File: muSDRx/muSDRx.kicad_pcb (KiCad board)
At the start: 2 copper layers, 100 x 100 mm, 98 parts, among them CON1 SJ1-3523N, CON2 SJ1-3523N, J1 Conn_01x02_Male, J11 Conn_01x02_Male, J2 Conn_01x02_Male, J3 Conn_01x02_Male, J4 Conn_01x02_Male, J5 Conn_01x02_Male, J6 Conn_01x02_Male, J9 Conn_01x04_Male, P1 BNC, Q1 MMBT2222A-TP, SW1 SW_Push, SW2 SW_Push, SW3 Rotary_Encoder_Switch, U1 LCD1602, U2 Si5351A-B-GT, U3 SN74CBT3253, U4 BluePill, U5 LT6231 (or LM4562), U6 MC78M05_TO252, Y1 CX3225

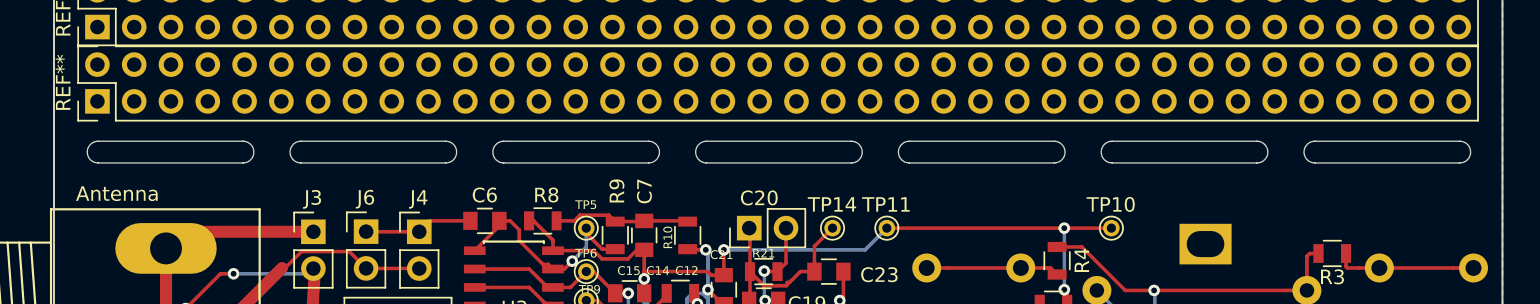
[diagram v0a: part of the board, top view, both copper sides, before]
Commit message: Added notes and C11-C15 value changes.
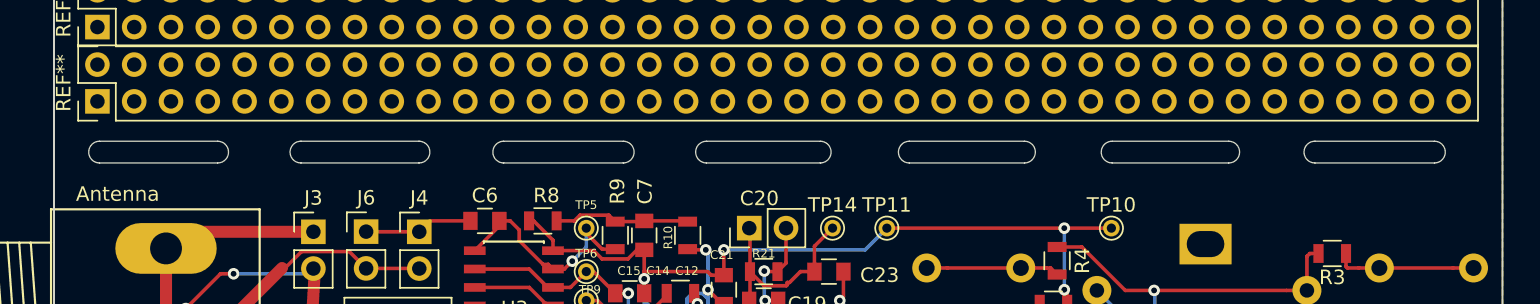
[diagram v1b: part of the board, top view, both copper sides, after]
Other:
- outline, holes or cut-outs redrawn
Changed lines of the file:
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@@
     (pad_to_mask_clearance 0.051)
     (solder_mask_min_width 0.25)
+    (pad_to_paste_clearance_ratio -0.2)
     (aux_axis_origin 0 0)
     (visible_elements FFFFFF7F)
@@
       (outputformat 1)
       (mirror false)
-      (drillshape 1)
+      (drillshape 0)
       (scaleselection 1)
       (outputdirectory ""))
@@
     )
   )
+  (gr_arc (start 61.3 95.5) (end 61.3 96.25) (angle -180) (layer Edge.Cuts) (width 0.05))
   (gr_text "Sound card" (at 144.9 113.3) (layer F.SilkS)
     (effects (font (size 1 1) (thickness 0.15)))
@@
   (gr_line (start 150 50) (end 150 150) (layer F.SilkS) (width 0.12))
   (gr_line (start 50 50) (end 150 50) (layer F.SilkS) (width 0.12))
-  (gr_arc (start 147.05 95.5) (end 147.05 96.25) (angle -180) (layer Edge.Cuts) (width 0.05))
+  (gr_arc (start 145.3 95.5) (end 145.3 96.25) (angle -180) (layer Edge.Cuts) (width 0.05))
   (gr_arc (start 137.05 95.5) (end 137.05 94.75) (angle -180) (layer Edge.Cuts) (width 0.05))
-  (gr_line (start 147.05 94.75) (end 137.05 94.75) (layer Edge.Cuts) (width 0.05))
-  (gr_line (start 137.05 96.25) (end 147.05 96.25) (layer Edge.Cuts) (width 0.05))
+  (gr_line (start 145.3 94.75) (end 137.05 94.75) (layer Edge.Cuts) (width 0.05))
+  (gr_line (start 137.05 96.25) (end 145.3 96.25) (layer Edge.Cuts) (width 0.05))
   (gr_arc (start 123.05 95.5) (end 123.05 94.75) (angle -180) (layer Edge.Cuts) (width 0.05))
-  (gr_line (start 133.05 94.75) (end 123.05 94.75) (layer Edge.Cuts) (width 0.05))
-  (gr_arc (start 133.05 95.5) (end 133.05 96.25) (angle -180) (layer Edge.Cuts) (width 0.05))
-  (gr_line (start 123.05 96.25) (end 133.05 96.25) (layer Edge.Cuts) (width 0.05))
+  (gr_line (start 131.1 94.75) (end 123.05 94.75) (layer Edge.Cuts) (width 0.05))
+  (gr_arc (start 131.1 95.5) (end 131.1 96.25) (angle -180) (layer Edge.Cuts) (width 0.05))
+  (gr_line (start 123.05 96.25) (end 131.1 96.25) (layer Edge.Cuts) (width 0.05))
   (gr_arc (start 109.05 95.5) (end 109.05 94.75) (angle -180) (layer Edge.Cuts) (width 0.05))
-  (gr_arc (start 119.05 95.5) (end 119.05 96.25) (angle -180) (layer Edge.Cuts) (width 0.05))
-  (gr_line (start 119.05 94.75) (end 109.05 94.75) (layer Edge.Cuts) (width 0.05))
-  (gr_line (start 109.05 96.25) (end 119.05 96.25) (layer Edge.Cuts) (width 0.05))
-  (gr_arc (start 105.05 95.5) (end 105.05 96.25) (angle -180) (layer Edge.Cuts) (width 0.05))
-  (gr_line (start 105.05 94.75) (end 95.05 94.75) (layer Edge.Cuts) (width 0.05))
+  (gr_arc (start 117 95.5) (end 117 96.25) (angle -180) (layer Edge.Cuts) (width 0.05))
+  (gr_line (start 117 94.75) (end 109.05 94.75) (layer Edge.Cuts) (width 0.05))
+  (gr_line (start 109.05 96.25) (end 117 96.25) (layer Edge.Cuts) (width 0.05))
+  (gr_arc (start 102.9 95.5) (end 102.9 96.25) (angle -180) (layer Edge.Cuts) (width 0.05))
+  (gr_line (start 102.9 94.75) (end 95.05 94.75) (layer Edge.Cuts) (width 0.05))
   (gr_arc (start 95.05 95.5) (end 95.05 94.75) (angle -180) (layer Edge.Cuts) (width 0.05))
-  (gr_line (start 95.05 96.25) (end 105.05 96.25) (layer Edge.Cuts) (width 0.05))
+  (gr_line (start 95.05 96.25) (end 102.9 96.25) (layer Edge.Cuts) (width 0.05))
   (gr_arc (start 81.05 95.5) (end 81.05 94.75) (angle -180) (layer Edge.Cuts) (width 0.05))
-  (gr_line (start 81.05 96.25) (end 91.05 96.25) (layer Edge.Cuts) (width 0.05))
-  (gr_line (start 91.05 94.75) (end 81.05 94.75) (layer Edge.Cuts) (width 0.05))
-  (gr_arc (start 91.05 95.5) (end 91.05 96.25) (angle -180) (layer Edge.Cuts) (width 0.05))
-  (gr_line (start 67.05 96.25) (end 77.05 96.25) (layer Edge.Cuts) (width 0.05))
-  (gr_line (start 77.05 94.75) (end 67.05 94.75) (layer Edge.Cuts) (width 0.05))
+  (gr_line (start 81.05 96.25) (end 89.3 96.25) (layer Edge.Cuts) (width 0.05))
+  (gr_line (start 89.3 94.75) (end 81.05 94.75) (layer Edge.Cuts) (width 0.05))
+  (gr_arc (start 89.3 95.5) (end 89.3 96.25) (angle -180) (layer Edge.Cuts) (width 0.05))
+  (gr_line (start 67.05 96.25) (end 75.2 96.25) (layer Edge.Cuts) (width 0.05))
+  (gr_line (start 75.2 94.75) (end 67.05 94.75) (layer Edge.Cuts) (width 0.05))
   (gr_arc (start 67.05 95.5) (end 67.05 94.75) (angle -180) (layer Edge.Cuts) (width 0.05))
-  (gr_arc (start 77.05 95.5) (end 77.05 96.25) (angle -180) (layer Edge.Cuts) (width 0.05))
-  (gr_line (start 53.05 96.25) (end 63.05 96.25) (layer Edge.Cuts) (width 0.05))
-  (gr_arc (start 53.05 95.5) (end 53.05 94.75) (angle -180) (layer Edge.Cuts) (width 0.05))
-  (gr_line (start 63.05 94.75) (end 53.05 94.75) (layer Edge.Cuts) (width 0.05))
-  (gr_arc (start 63.05 95.5) (end 63.05 96.25) (angle -180) (layer Edge.Cuts) (width 0.05))
+  (gr_arc (start 75.2 95.5) (end 75.2 96.25) (angle -180) (layer Edge.Cuts) (width 0.05))
+  (gr_line (start 53.15 96.25) (end 61.3 96.25) (layer Edge.Cuts) (width 0.05))
+  (gr_arc (start 53.15 95.5) (end 53.15 94.75) (angle -180) (layer Edge.Cuts) (width 0.05))
+  (gr_line (start 61.3 94.75) (end 53.15 94.75) (layer Edge.Cuts) (width 0.05))
   (gr_line (start 50.5 100) (end 150 100) (layer Margin) (width 0.15))
   (gr_line (start 50 150) (end 50 50) (layer Edge.Cuts) (width 0.05))
@@
     (connect_pads (clearance 0.508))
     (min_thickness 0.254)
-    (fill yes (arc_segments 32) (thermal_gap 0.508) (thermal_bridge_width 0.508))
+    (fill (arc_segments 32) (thermal_gap 0.508) (thermal_bridge_width 0.508))
     (polygon
       (pts
@@
     (connect_pads (clearance 0.508))
     (min_thickness 0.254)
-    (fill yes (arc_segments 32) (thermal_gap 0.508) (thermal_bridge_width 0.508))
+    (fill (arc_segments 32) (thermal_gap 0.508) (thermal_bridge_width 0.508))
     (polygon
       (pts

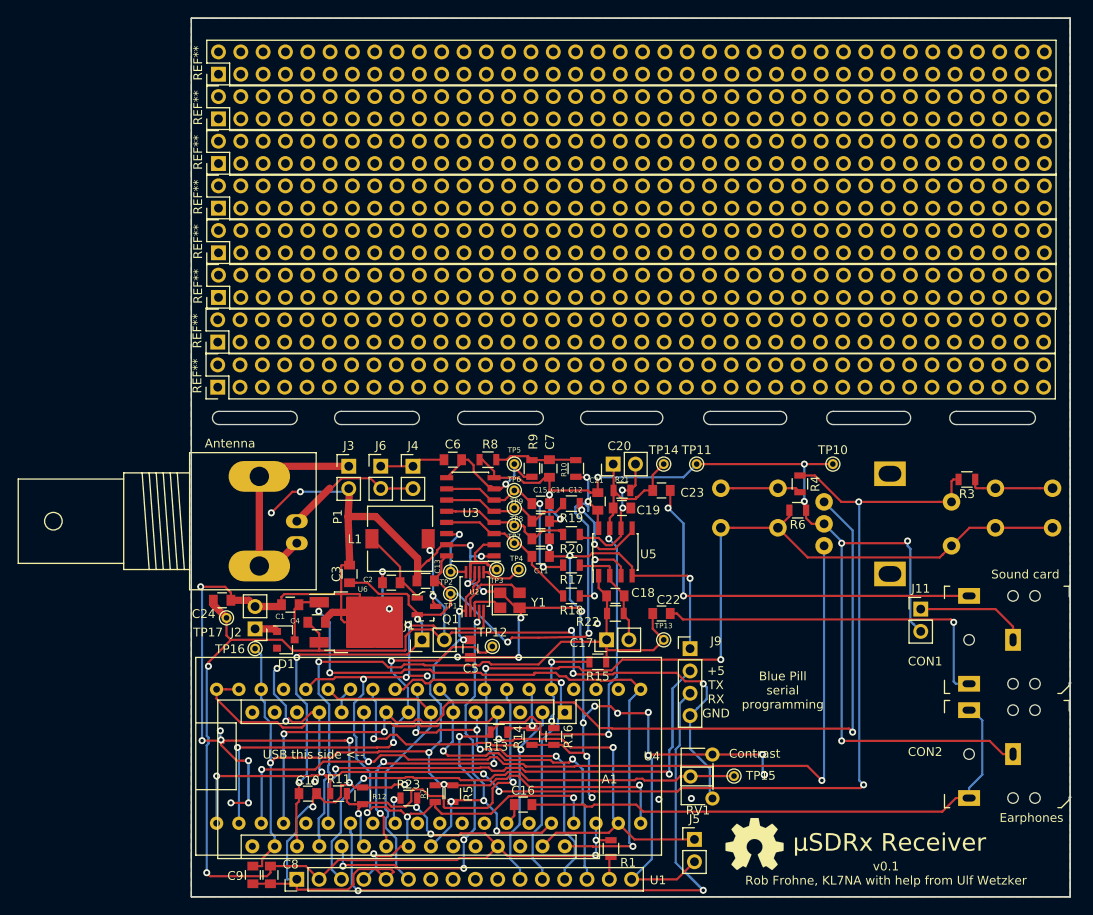
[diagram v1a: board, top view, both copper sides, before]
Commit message: Added v0.11 which fixed problems wit stand alone using Nano
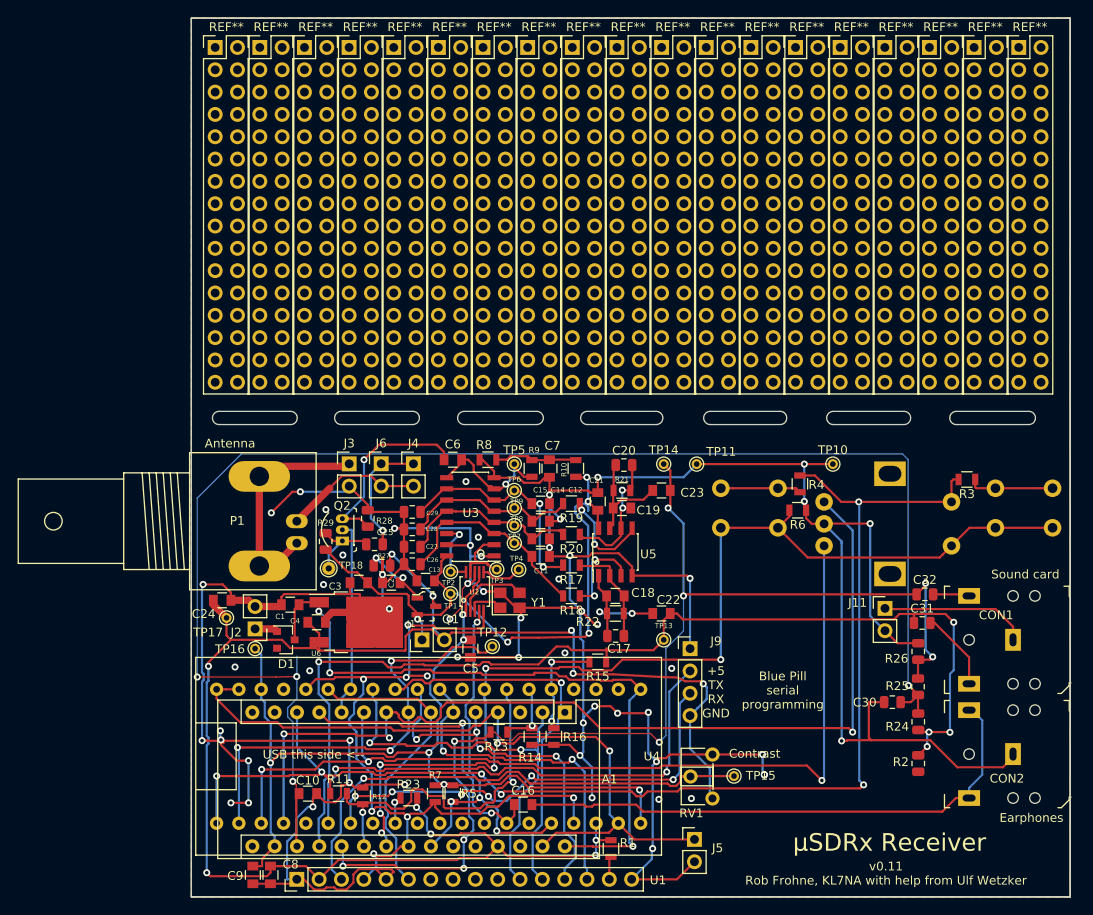
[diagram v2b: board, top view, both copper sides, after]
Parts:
- removed L1: 300uH, Inductors_SMD:L_7.3x7.3_H4.5
- removed the REF** at (53.1, 56.4)
- removed the REF** at (53.1, 61.5)
- removed the REF** at (53.1, 66.5)
- removed the REF** at (53.1, 71.6)
- removed the REF** at (53.1, 76.7)
- removed the REF** at (53.1, 81.8)
- removed the REF** at (53.0, 86.9)
- removed the REF** at (53.0, 92.0)
- removed REF***: OSHW-Symbol_6.7x6mm_SilkScreen, Symbols:OSHW-Symbol_6.7x6mm_SilkScreen
- added C25: 0.1uF, Capacitor_SMD:C_0805_2012Metric, F.Cu at (70.8, 109.9)
- added C26: 0.47u, Capacitor_SMD:C_0805_2012Metric, F.Cu at (75.1, 112.1)
- added C27: 0.47u, Capacitor_SMD:C_0805_2012Metric, F.Cu at (75.1, 110.2)
- added C28: 0.47u, Capacitor_SMD:C_0805_2012Metric, F.Cu at (75.1, 108.2)
- added C29: 0.47u, Capacitor_SMD:C_0805_2012Metric, F.Cu at (75.1, 106.2)
- added C30: 0.1uF, Capacitor_SMD:C_0805_2012Metric, F.Cu at (129.8, 127.8)
- added C31: 10uF, Capacitor_SMD:C_0805_2012Metric, F.Cu at (133.2, 118.8)
- added C32: 10uF, Capacitor_SMD:C_0805_2012Metric, F.Cu at (133.5, 115.6)
- added Q2: BS170, digikey-footprints:TO-92-3, F.Cu at (67.2, 109.5)
- added R2: 10k, Resistor_SMD:R_0805_2012Metric, F.Cu at (132.7, 134.8)
- added R24: 10k, Resistor_SMD:R_0805_2012Metric, F.Cu at (132.7, 130.1)
- added R25: 10k, Resistor_SMD:R_0805_2012Metric, F.Cu at (132.7, 126.1)
- added R26: 10k, Resistor_SMD:R_0805_2012Metric, F.Cu at (132.7, 122.1)
- added R27: 1k, Resistor_SMD:R_0805_2012Metric, F.Cu at (71.7, 112.3)
- added R28: 1k, Resistor_SMD:R_0805_2012Metric, F.Cu at (70.1, 106.9)
- added R29: 1M, Resistor_SMD:R_0805_2012Metric, F.Cu at (65.3, 109.5)
- added REF**: PinHeader_2x16_P2.54mm_Vertical, Connector_PinHeader_2.54mm:PinHeader_2x16_P2.54mm_Vertical, F.Cu at (52.7, 53.3)
- added REF**: PinHeader_2x16_P2.54mm_Vertical, Connector_PinHeader_2.54mm:PinHeader_2x16_P2.54mm_Vertical, F.Cu at (108.6, 53.3)
- added REF**: PinHeader_2x16_P2.54mm_Vertical, Connector_PinHeader_2.54mm:PinHeader_2x16_P2.54mm_Vertical, F.Cu at (103.5, 53.3)
- added REF**: PinHeader_2x16_P2.54mm_Vertical, Connector_PinHeader_2.54mm:PinHeader_2x16_P2.54mm_Vertical, F.Cu at (98.4, 53.3)
- added REF**: PinHeader_2x16_P2.54mm_Vertical, Connector_PinHeader_2.54mm:PinHeader_2x16_P2.54mm_Vertical, F.Cu at (93.3, 53.3)
- added REF**: PinHeader_2x16_P2.54mm_Vertical, Connector_PinHeader_2.54mm:PinHeader_2x16_P2.54mm_Vertical, F.Cu at (88.3, 53.3)
- added REF**: PinHeader_2x16_P2.54mm_Vertical, Connector_PinHeader_2.54mm:PinHeader_2x16_P2.54mm_Vertical, F.Cu at (83.2, 53.3)
- added REF**: PinHeader_2x16_P2.54mm_Vertical, Connector_PinHeader_2.54mm:PinHeader_2x16_P2.54mm_Vertical, F.Cu at (78.1, 53.3)
- added REF**: PinHeader_2x16_P2.54mm_Vertical, Connector_PinHeader_2.54mm:PinHeader_2x16_P2.54mm_Vertical, F.Cu at (73.0, 53.3)
- added REF**: PinHeader_2x16_P2.54mm_Vertical, Connector_PinHeader_2.54mm:PinHeader_2x16_P2.54mm_Vertical, F.Cu at (68.0, 53.3)
- added REF**: PinHeader_2x16_P2.54mm_Vertical, Connector_PinHeader_2.54mm:PinHeader_2x16_P2.54mm_Vertical, F.Cu at (62.9, 53.3)
- added REF**: PinHeader_2x16_P2.54mm_Vertical, Connector_PinHeader_2.54mm:PinHeader_2x16_P2.54mm_Vertical, F.Cu at (57.8, 53.3)
- added REF**: PinHeader_2x16_P2.54mm_Vertical, Connector_PinHeader_2.54mm:PinHeader_2x16_P2.54mm_Vertical, F.Cu at (144.2, 53.3)
- added REF**: PinHeader_2x16_P2.54mm_Vertical, Connector_PinHeader_2.54mm:PinHeader_2x16_P2.54mm_Vertical, F.Cu at (139.1, 53.3)
- added REF**: PinHeader_2x16_P2.54mm_Vertical, Connector_PinHeader_2.54mm:PinHeader_2x16_P2.54mm_Vertical, F.Cu at (134.0, 53.3)
- added REF**: PinHeader_2x16_P2.54mm_Vertical, Connector_PinHeader_2.54mm:PinHeader_2x16_P2.54mm_Vertical, F.Cu at (128.9, 53.3)
- added REF**: PinHeader_2x16_P2.54mm_Vertical, Connector_PinHeader_2.54mm:PinHeader_2x16_P2.54mm_Vertical, F.Cu at (123.8, 53.3)
- added REF**: PinHeader_2x16_P2.54mm_Vertical, Connector_PinHeader_2.54mm:PinHeader_2x16_P2.54mm_Vertical, F.Cu at (118.8, 53.3)
- added REF**: PinHeader_2x16_P2.54mm_Vertical, Connector_PinHeader_2.54mm:PinHeader_2x16_P2.54mm_Vertical, F.Cu at (113.7, 53.3)
- added TP18: TestPoint, TestPoint:TestPoint_THTPad_D1.5mm_Drill0.7mm, F.Cu at (65.6, 112.6)
- C11, C12, C14, C15: value 0.47uF -> 0.01uF
- C17, C20: footprint Pin_Headers:Pin_Header_Straight_1x02_Pitch2.54mm -> Capacitor_SMD:C_0805_2012Metric
- R18, R19: value 100 -> 0
- R5, R7: value 1k -> 4.7k
- moved J11 4.07 mm to (128.9, 117.2)
- moved C3 1.46 mm to (69.1, 114.2), turned to 180 degrees
- moved C20 1.23 mm to (99.2, 100.9), turned to 0 degrees
- moved C17 1.12 mm to (98.3, 120.3), turned to 0 degrees
- moved J3 0.28 mm to (68.0, 100.7)
- moved J6 0.28 mm to (71.6, 100.7)
- moved J4 0.28 mm to (75.3, 100.7)
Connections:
- A1 pad 12: /VHI -> /AUD_OUT
- A1 pad 13: (no net) -> /VHI
- A1 pad 18: +4.3V -> /AREF
- C10 pad 1: +4.3V -> /AREF
- C16 pad 2: Net-(C16-Pad2) -> /AUD_OUT
- C17 pad 1: /AUD_0 -> Net-(C17-Pad1)
- C18 pad 1: /AUD_0 -> Net-(C17-Pad1)
- C19 pad 1: /AUD_1 -> Net-(C19-Pad1)
- C20 pad 1: /AUD_1 -> Net-(C19-Pad1)
- C22 pad 1: Net-(C22-Pad1) -> /AUD_0
- C22 pad 2: /AUD_0 -> Net-(C17-Pad1)
- C23 pad 1: Net-(C23-Pad1) -> /AUD_1
- C23 pad 2: /AUD_1 -> Net-(C19-Pad1)
- CON1 pad 2: Net-(C23-Pad1) -> Net-(C32-Pad2)
- CON1 pad 3: Net-(C22-Pad1) -> Net-(C31-Pad2)
- J4 pad 1: Net-(C6-Pad2) -> Net-(C25-Pad2)
- J6 pad 1: Net-(C6-Pad2) -> Net-(C25-Pad2)
- R21 pad 1: /AUD_1 -> Net-(C19-Pad1)
- R22 pad 1: /AUD_0 -> Net-(C17-Pad1)
- U4 pad PB6: Net-(C16-Pad2) -> /AUD_OUT
- U5 pad 1: /AUD_0 -> Net-(C17-Pad1)
- U5 pad 7: /AUD_1 -> Net-(C19-Pad1)
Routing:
- net /AREF: track 0.00 -> 171.5 mm, vias 0 -> 4
- net Net-(C23-Pad1): track 45.3 -> 0.00 mm, vias 2 -> 0
- net /AUD_0: track 77.6 -> 122.4 mm, vias 1 -> 5
- net Net-(C22-Pad1): track 41.3 -> 0.00 mm, vias 1 -> 0
- net /AUD_1: track 92.8 -> 132.0 mm, vias 6 -> 9
- net /AUD_OUT: track 0.00 -> 34.1 mm, vias 0 -> 2
- net +4.3V: track 107.2 -> 73.9 mm, vias 7 -> 5
- net Net-(J9-Pad3): track 74.8 -> 52.4 mm, vias 2 -> 6
- net /RX: track 3.04 -> 22.3 mm
- net GND: track 473.6 -> 490.9 mm, vias 48 -> 59
- net Net-(C25-Pad2): track 0.00 -> 15.0 mm, vias 0 -> 1
- net Net-(C6-Pad2): track 7.51 -> 22.0 mm, vias 0 -> 1
- net Net-(C17-Pad1): track 0.00 -> 14.3 mm, vias 0 -> 2
- net Net-(C19-Pad1): track 0.00 -> 12.8 mm
- net Net-(C31-Pad2): track 0.00 -> 9.03 mm
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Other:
- rule trace_min: 0.2 -> 0.128
- board text added: "v0.11 Rob Frohne, KL7NA with help from Ulf Wetzker"
- board text added: "µSDRx Receiver, v0.11 After µSDX, by PE1NNZ Rob Frohne KL7NA with help from Ulf Wetzker"
- board text removed: "v0.1 Rob Frohne, KL7NA with help from Ulf Wetzker"
- board text removed: "µSDRx Receiver, v0.1 After µSDX, by PE1NNZ Rob Frohne KL7NA with help from Ulf Wetzker"

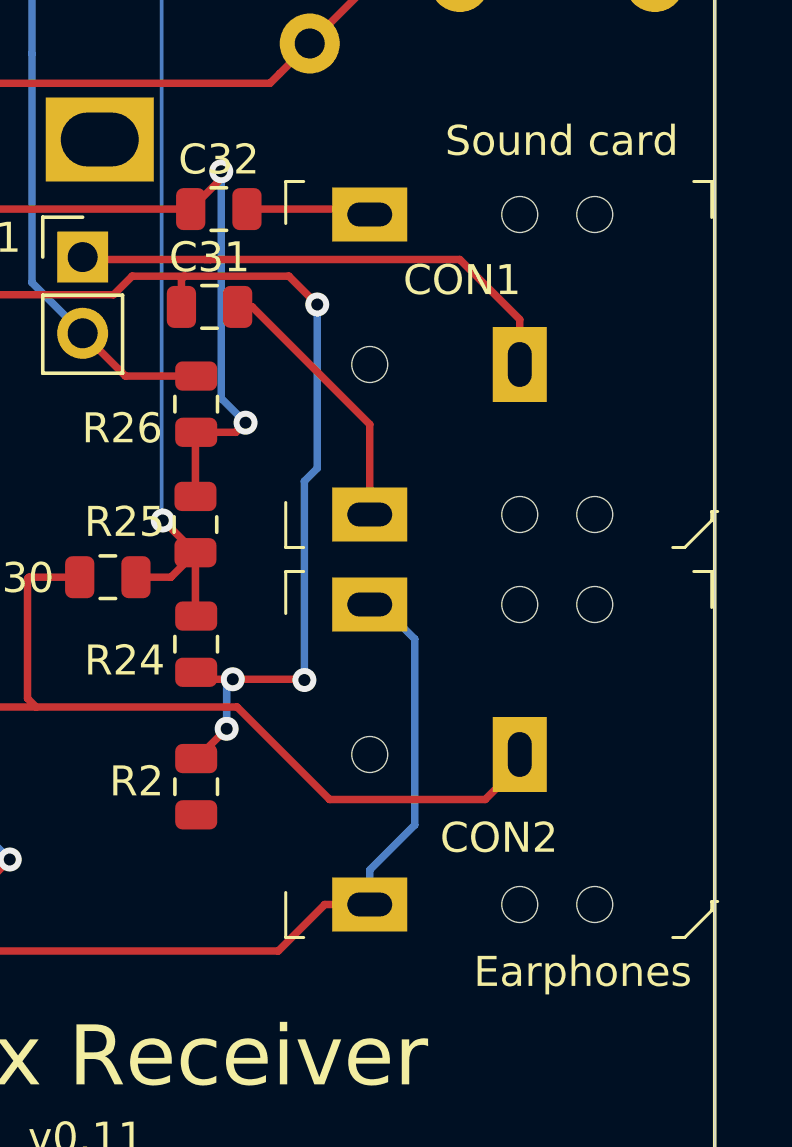
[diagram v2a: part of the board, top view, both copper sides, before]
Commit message: Fixed 3.5mm jack footprints so switched ones will work.
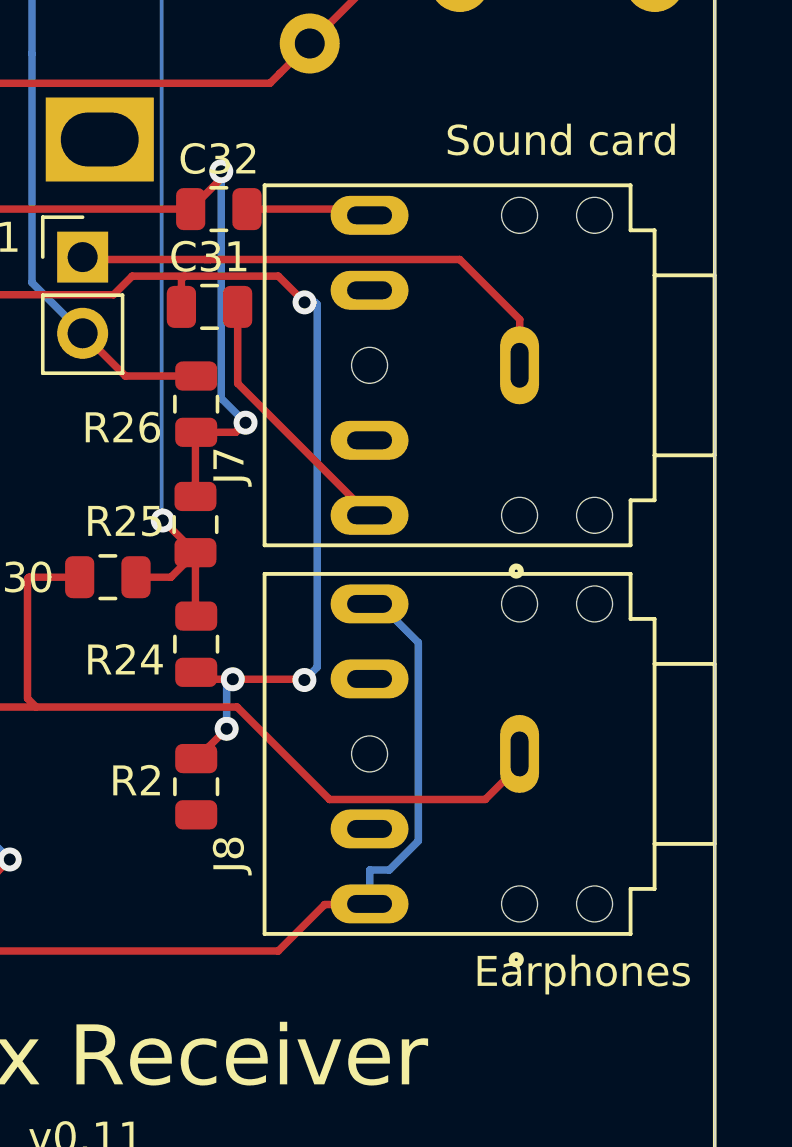
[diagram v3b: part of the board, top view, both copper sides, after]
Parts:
- removed CON1, CON2: SJ1-3523N, digikey-footprints:Headphone_Jack_2.5mm_SJ1-3523N
- added J7: 35RAPC4BHN2, muSDRx:SWITCHCRAFT_35RAPC4BHN2, F.Cu at (142.5, 120.8)
- added J8: 35RAPC4BHN2, muSDRx:SWITCHCRAFT_35RAPC4BHN2, F.Cu at (142.5, 133.7)
- C22, C23, C31, C32: value 10uF -> 1uF

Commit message: So I could change branches.
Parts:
- removed J7, J8: 35RAPC4BHN2, muSDRx:SWITCHCRAFT_35RAPC4BHN2
- added CON1: SJ1-3523N, digikey-footprints:Headphone_Jack_2.5mm_SJ1-3523N, F.Cu at (138.5, 120.8)
- added CON2: SJ1-3523N, digikey-footprints:Headphone_Jack_2.5mm_SJ1-3523N, F.Cu at (138.5, 133.8)
- C22, C23, C31, C32: value 1uF -> 10uF
